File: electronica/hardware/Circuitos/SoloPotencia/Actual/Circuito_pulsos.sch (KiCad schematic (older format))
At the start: 33 parts, among them J3 Conn_01x03, J4 ACS712, P3 SALIDA_1, P4 SALIDA_2, Q10 IRF4905, Q11 IRFZ46N, Q12 IRF4905, Q13 IRFZ46N, Q14 2N2222, Q9 2N2222

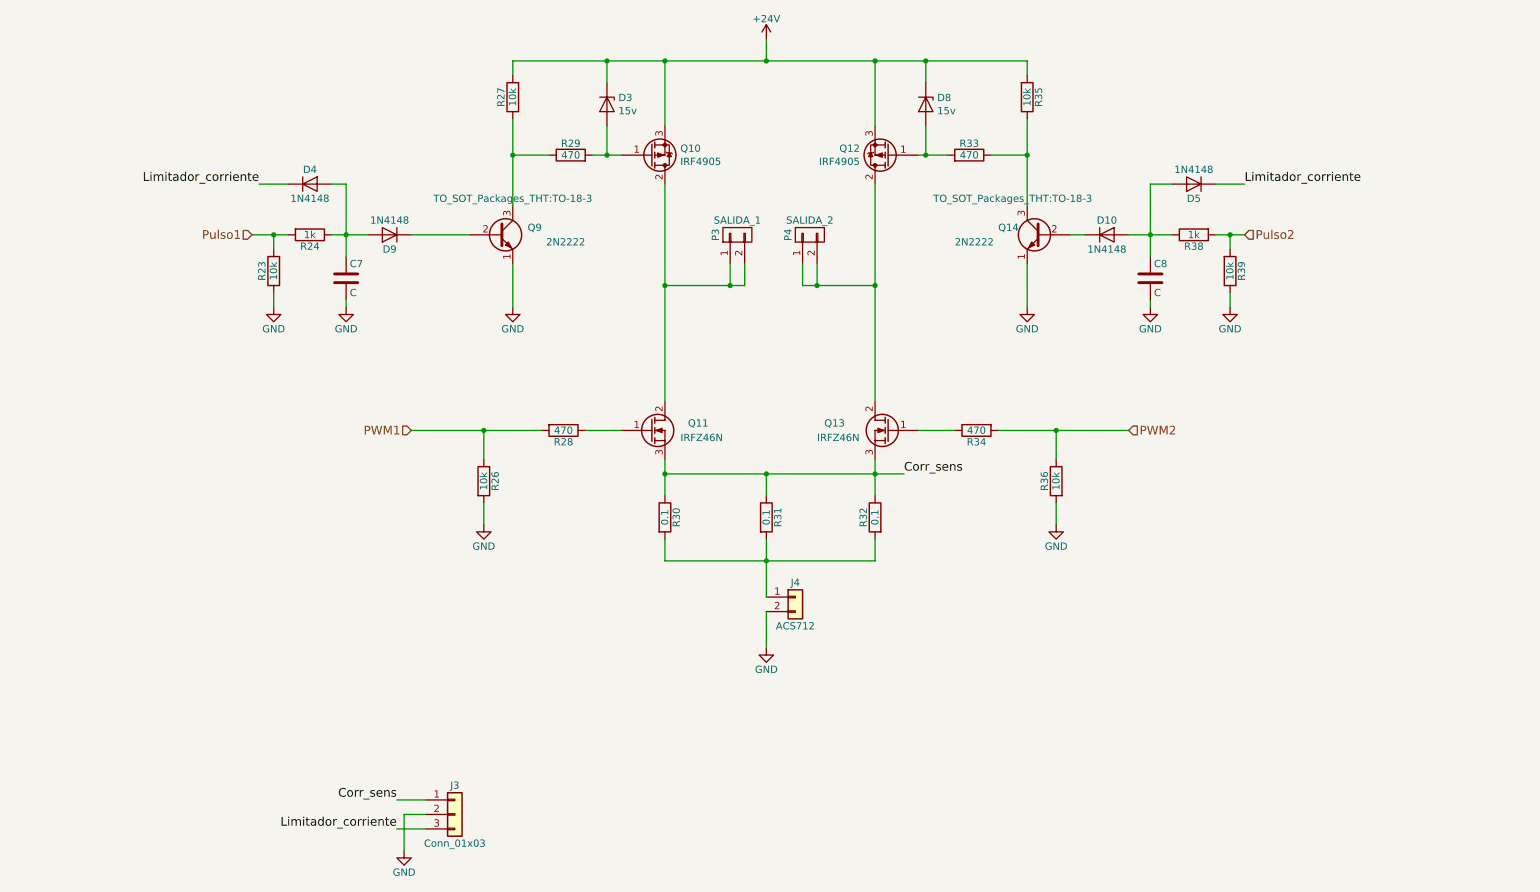
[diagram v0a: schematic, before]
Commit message: Se agregaron mediciones con el nuevo driver para el transistor PMOS
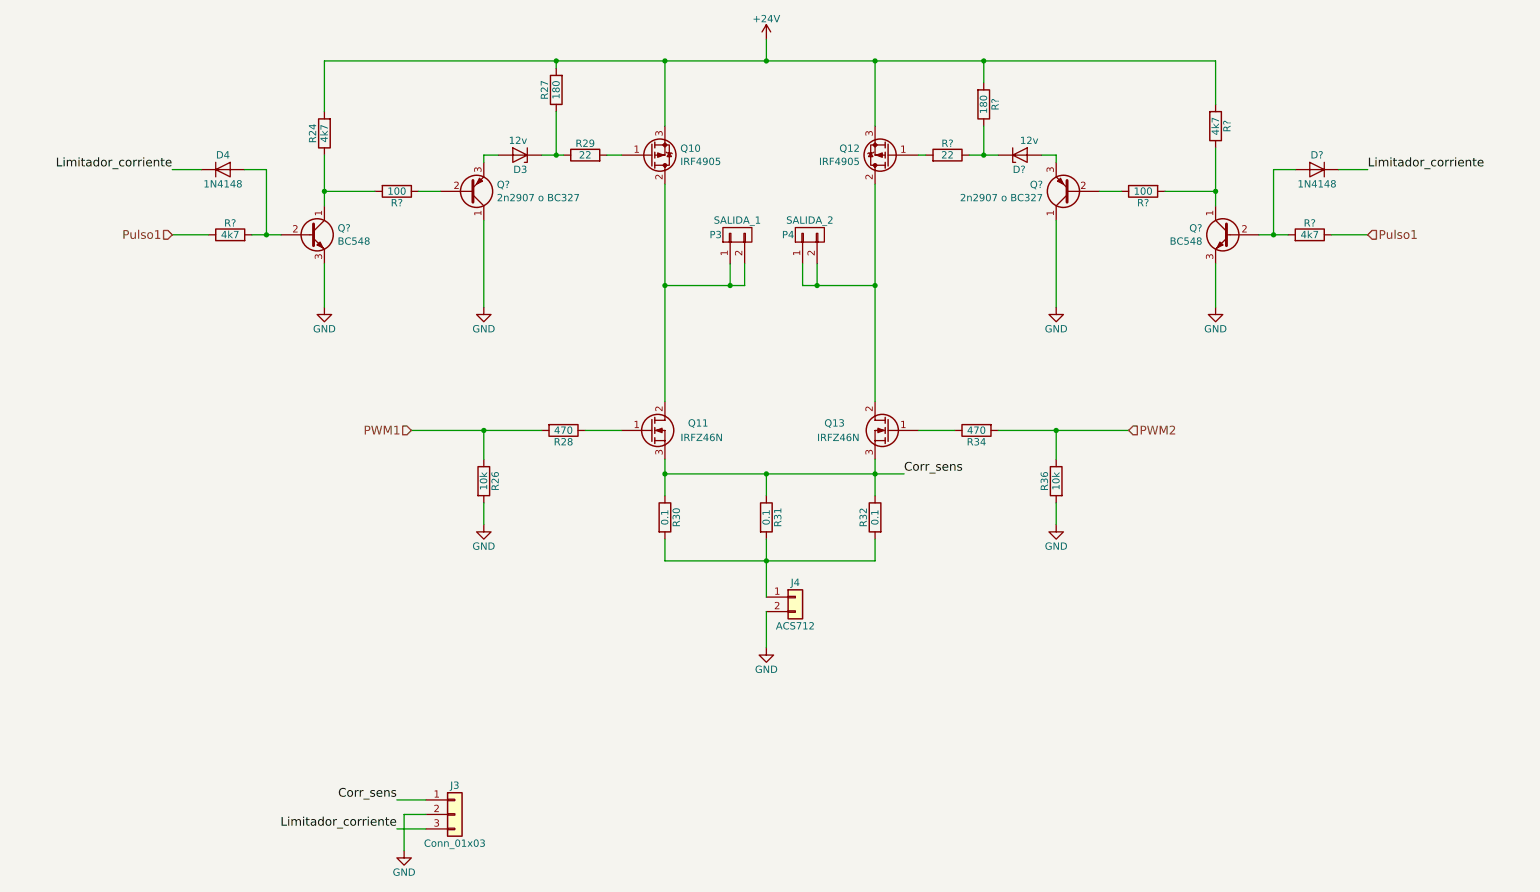
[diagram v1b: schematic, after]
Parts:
- removed C7, C8: C, Capacitors_THT:C_Disc_D5.0mm_W2.5mm_P2.50mm, symbol FuenteDePulsos-rescue:C
- removed D10, D5, D9: 1N4148, Diodes_THT:D_A-405_P7.62mm_Horizontal, symbol FuenteDePulsos-rescue:D
- removed D8: 15v, Diodes_THT:D_A-405_P7.62mm_Horizontal, symbol Device:D_Zener
- removed Q14, Q9: 2N2222, TO_SOT_Packages_THT:TO-18-3, symbol FuenteDePulsos-rescue:2N2222
- removed R23, R35, R39: 10k, Resistors_THT:R_Axial_DIN0207_L6.3mm_D2.5mm_P7.62mm_Horizontal, symbol FuenteDePulsos-rescue:R
- removed R33: 470, Resistors_THT:R_Axial_DIN0207_L6.3mm_D2.5mm_P7.62mm_Horizontal, symbol FuenteDePulsos-rescue:R
- removed R38: 1k, Resistors_THT:R_Axial_DIN0207_L6.3mm_D2.5mm_P7.62mm_Horizontal, symbol FuenteDePulsos-rescue:R
- added D?: 1N4148, Diodes_THT:D_A-405_P7.62mm_Horizontal, symbol FuenteDePulsos-rescue:D
- added D?: 12v, Diodes_THT:D_A-405_P7.62mm_Horizontal, symbol Device:D_Zener
- added Q? (x2): 2n2907 o BC327, Package_TO_SOT_THT:TO-92_Inline_Wide, symbol Device:Q_PNP_CBE
- added Q? (x2): BC548, Package_TO_SOT_THT:TO-92_Inline_Wide, symbol Transistor_BJT:BC548
- added R? (x2): 100, Resistors_THT:R_Axial_DIN0207_L6.3mm_D2.5mm_P7.62mm_Horizontal, symbol FuenteDePulsos-rescue:R
- added R? (x3): 4k7, Resistors_THT:R_Axial_DIN0207_L6.3mm_D2.5mm_P7.62mm_Horizontal, symbol FuenteDePulsos-rescue:R
- added R?: 180, Resistors_THT:R_Axial_DIN0207_L6.3mm_D2.5mm_P7.62mm_Horizontal, symbol FuenteDePulsos-rescue:R
- added R?: 22, Resistors_THT:R_Axial_DIN0207_L6.3mm_D2.5mm_P7.62mm_Horizontal, symbol FuenteDePulsos-rescue:R
- D3: value 15v -> 12v
- R24: value 1k -> 4k7
- R27: value 10k -> 180
- R29: value 470 -> 22
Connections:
- net +24V: now also R24.2, R?.2, R?.2; no longer D3.1 (K)
- net GND: now also Q?.1 (C), Q?.1 (C), Q?.3 (E), Q?.3 (E)
- net Limitador_corriente: now also D?.1 (K)
- net Pulso1: now also R?.1, R?.1; no longer R24.2
- net at R24.1: now also Q?.1 (C), R?.2; no longer D4.2 (A)
- net at R27.1, R29.1: now also D3.1 (K)
- net at Q10.1 (G), R29.2: no longer D3.2 (A)
- net at Q12.1 (G): now also R?.2
- new net: D4.2 (A), Q?.2 (B), R?.2
- new net: D3.2 (A), Q?.3 (E)
- new net: Q?.2 (B), R?.1 (x2)
- new net: D?.1 (K), R?.1, R?.1
- new net: D?.2 (A), Q?.2 (B), R?.2
- new net: D?.2 (A), Q?.3 (E)
- new net: Q?.1 (C), R?.1, R?.2
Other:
- moved on the sheet: D3, D4, R24, R27, R29
